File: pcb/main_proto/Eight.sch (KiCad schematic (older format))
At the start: 29 parts, among them IC1 ATMEGA328-A, P1 DISP, P2 PWR, P3 POT, P4 SDISP, P5 SPK, P6 ISP, P7 BTN, U1 ULN2003, U2 LM2931Z-3.3/5.0, U3 LM386, Y1 16Mhz

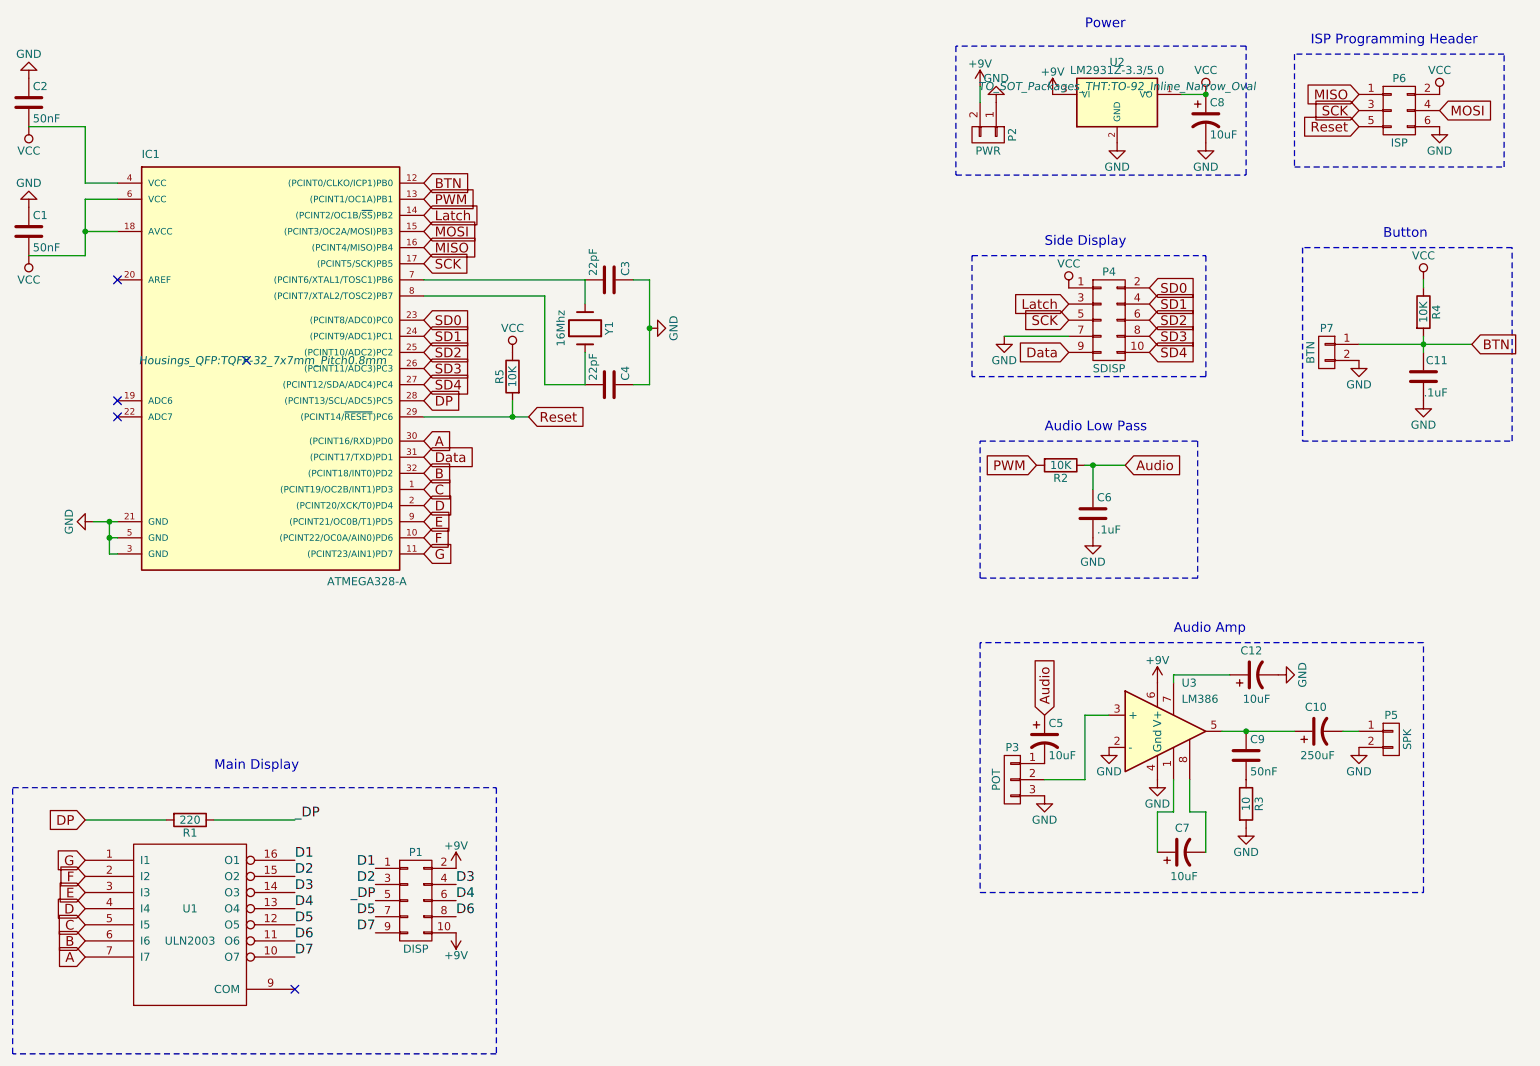
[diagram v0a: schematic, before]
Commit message: Fix: Lyout of power section on the schematics.
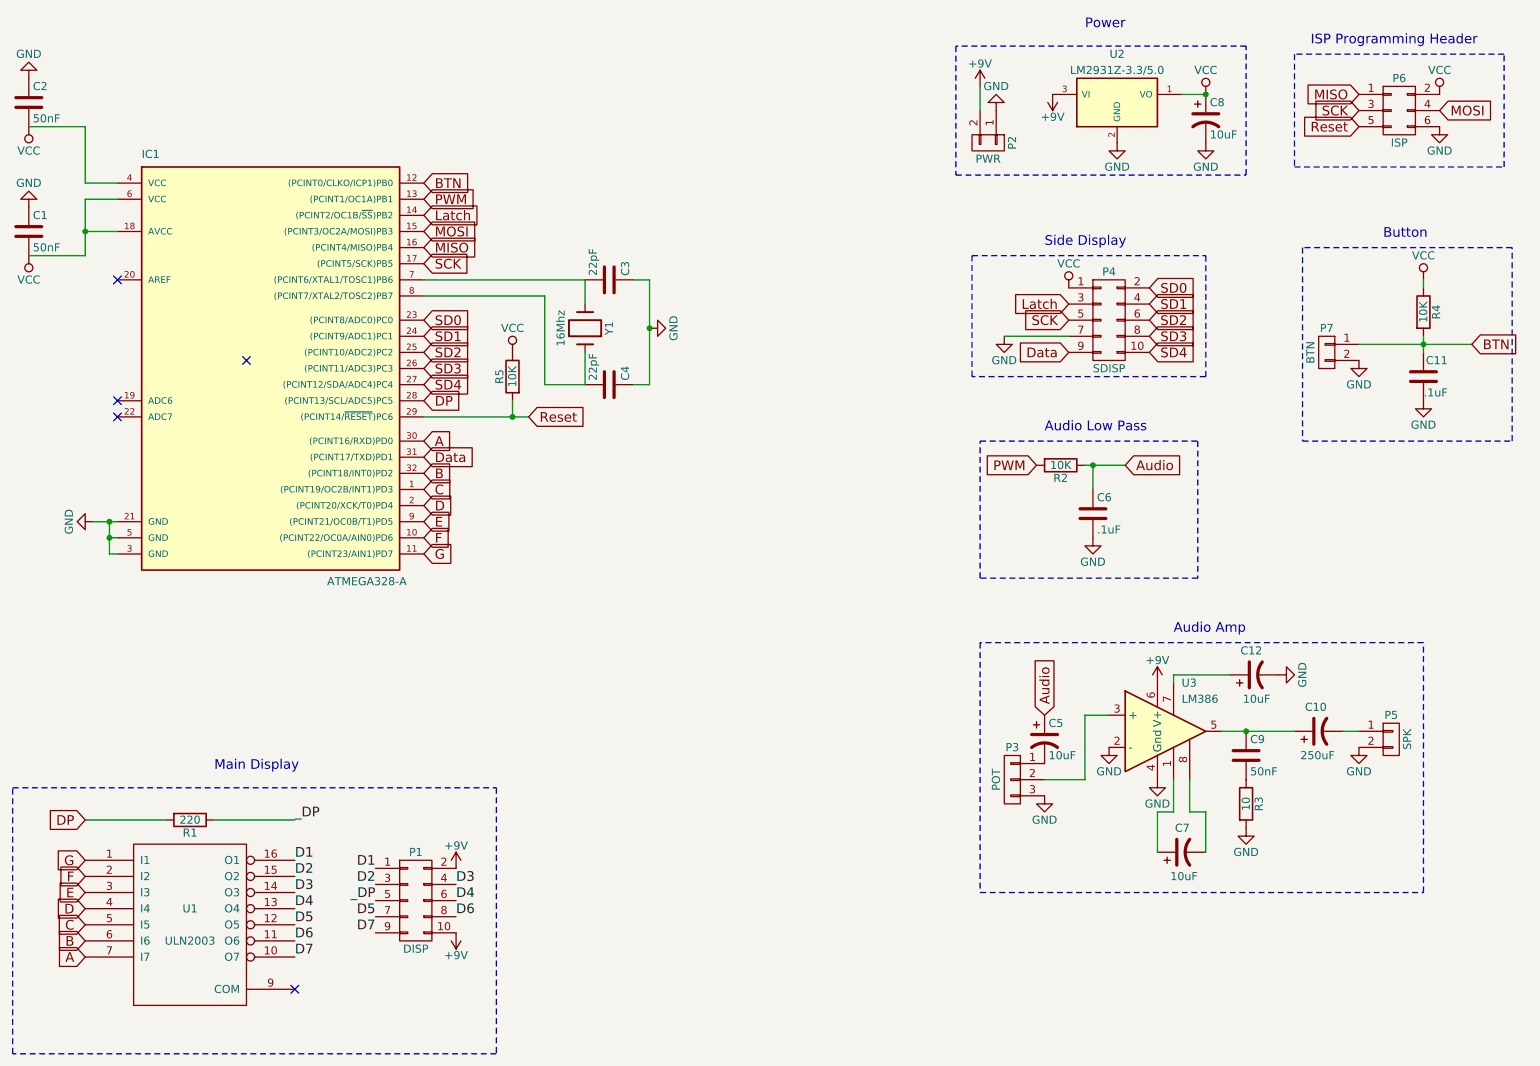
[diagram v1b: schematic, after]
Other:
- moved on the sheet: P2
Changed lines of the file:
@@
 LIBS:valves
 LIBS:lm386_bypass
+LIBS:Eight-cache
 EELAYER 25 0
 EELAYER END
@@
 	5350 2300 5450 2300
 Wire Wire Line
-	5450 2300 5450 2950
+	5450 2300 5450 2600
+Wire Wire Line
+	5450 2600 5450 2950
 Wire Wire Line
 	5450 2950 5350 2950
@@
 $EndComp
 Wire Wire Line
-	4050 3150 4700 3150
+	4050 3150 4600 3150
+Wire Wire Line
+	4600 3150 4700 3150
 Text GLabel 4700 3150 2    60   Input ~ 0
 Reset
@@
 $EndComp
 Wire Wire Line
-	8150 3450 8400 3450
+	8150 3450 8200 3450
+Wire Wire Line
+	8200 3450 8400 3450
 Wire Wire Line
 	8200 3450 8200 3600
@@
 $EndComp
 Wire Wire Line
-	9000 5100 9450 5100
+	9000 5100 9150 5100
+Wire Wire Line
+	9150 5100 9450 5100
 Wire Wire Line
 	9750 5100 9850 5100
@@
 F 3 "" H 7950 1150 50  0000 C CNN
 	1    7950 1150
-	1    0    0    -1
+	-1   0    0    1
 $EndComp
 $Comp
@@
 L CONN_01X02 P2
 U 1 1 566A1E71
-P 7550 1400
-F 0 "P2" H 7550 1550 50  0000 C CNN
-F 1 "PWR" V 7650 1400 50  0000 C CNN
-F 2 "Pin_Headers:Pin_Header_Straight_1x02" H 7550 1400 50  0001 C CNN
-F 3 "" H 7550 1400 50  0000 C CNN
-	1    7550 1400
+P 7550 1450
+F 0 "P2" H 7550 1600 50  0000 C CNN
+F 1 "PWR" V 7650 1450 50  0000 C CNN
+F 2 "Pin_Headers:Pin_Header_Straight_1x02" H 7550 1450 50  0001 C CNN
+F 3 "" H 7550 1450 50  0000 C CNN
+	1    7550 1450
 	0    1    1    0
 $EndComp
@@
 L GND #PWR020
 U 1 1 566A202F
-P 7600 1200
-F 0 "#PWR020" H 7600 950 50  0001 C CNN
-F 1 "GND" H 7600 1050 50  0000 C CNN
-F 2 "" H 7600 1200 50  0000 C CNN
-F 3 "" H 7600 1200 50  0000 C CNN
-	1    7600 1200
+P 7600 1250
+F 0 "#PWR020" H 7600 1000 50  0001 C CNN
+F 1 "GND" H 7600 1100 50  0000 C CNN
+F 2 "" H 7600 1250 50  0000 C CNN
+F 3 "" H 7600 1250 50  0000 C CNN
+	1    7600 1250
 	-1   0    0    1
 $EndComp
 Wire Wire Line
-	7500 1100 7500 1200
+	7500 1100 7500 1250
 $Comp
 L +9V #PWR021
@@
 F 0 "IC1" H 2300 4050 50  0000 L BNN
 F 1 "ATMEGA328-A" H 3450 1400 50  0000 L BNN
-F 2 "Housings_QFP:TQFP-32_7x7mm_Pitch0.8mm" H 3050 2800 50  0000 C CIN
+F 2 "Housings_QFP:TQFP-32_7x7mm_Pitch0.8mm" H 3050 2800 50  0001 C CIN
 F 3 "" H 3050 2800 50  0000 C CNN
 	1    3050 2800
@@
 	1600 1350 1950 1350
 Wire Wire Line
-	1950 1800 1950 2150
+	1950 1800 1950 2000
+Wire Wire Line
+	1950 2000 1950 2150
 Wire Wire Line
 	1950 1800 2150 1800
@@
 Connection ~ 1950 2000
 Wire Wire Line
-	2000 3800 2150 3800
-Wire Wire Line
-	2100 3800 2100 4000
+	2000 3800 2100 3800
+Wire Wire Line
+	2100 3800 2150 3800
+Wire Wire Line
+	2100 3800 2100 3900
+Wire Wire Line
+	2100 3900 2100 4000
 Wire Wire Line
 	2100 4000 2150 4000
@@
 $EndComp
 Wire Wire Line
-	9850 2700 10550 2700
-Wire Wire Line
-	10250 2650 10250 2750
+	9850 2700 10250 2700
+Wire Wire Line
+	10250 2700 10550 2700
+Wire Wire Line
+	10250 2650 10250 2700
+Wire Wire Line
+	10250 2700 10250 2750
 Connection ~ 10250 2700
 Wire Wire Line
@@
 U 1 1 5696F484
 P 8350 1200
-F 0 "U2" H 8350 1450 50  0000 C CNN
+F 0 "U2" H 8350 1500 50  0000 C CNN
 F 1 "LM2931Z-3.3/5.0" H 8350 1400 50  0000 C CNN
-F 2 "TO_SOT_Packages_THT:TO-92_Inline_Narrow_Oval" H 8350 1300 50  0000 C CIN
+F 2 "TO_SOT_Packages_THT:TO-92_Inline_Narrow_Oval" H 8350 1300 50  0001 C CIN
 F 3 "" H 8350 1200 50  0000 C CNN
 	1    8350 1200
